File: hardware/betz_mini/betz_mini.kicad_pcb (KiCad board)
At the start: 2 copper layers, 17 parts, among them U1 stm32g474ceu6, U2 AS5047U, U3 IIS328DQ, U4 MP6540

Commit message: WIP
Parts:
- removed R5: 4k7, Resistor_SMD:R_0402_1005Metric
- added C7: 15p, Capacitor_SMD:C_0402_1005Metric, F.Cu at (144.5, 98.5)
- added C8: 100n, Capacitor_SMD:C_0402_1005Metric, F.Cu at (145.5, 85.5)
- added H1: MountingHole_Pad, MountingHole:MountingHole_2.2mm_M2_DIN965_Pad, F.Cu at (140.0, 90.0)
- added H2: MountingHole_Pad, MountingHole:MountingHole_2.2mm_M2_DIN965_Pad, F.Cu at (160.0, 90.0)
- added H3: MountingHole_Pad, MountingHole:MountingHole_2.2mm_M2_DIN965_Pad, F.Cu at (140.0, 110.0)
- added H4: MountingHole_Pad, MountingHole:MountingHole_2.2mm_M2_DIN965_Pad, F.Cu at (160.0, 110.0)
- added J1: upstairs, Connector_PinHeader_2.00mm:PinHeader_2x06_P2.00mm_Vertical, F.Cu at (135.5, 95.0)
- added J2: Conn_ARM_JTAG_SWD_10, Connector_PinHeader_1.27mm:PinHeader_2x05_P1.27mm_Vertical, F.Cu at (152.5, 84.5)
- added X1: 8 MHz, Crystal:Crystal_SMD_5032-2Pin_5.0x3.2mm, F.Cu at (142.0, 97.0)
- C4, C5: value 10u -> 22u
- C6: value 10u -> 15p; footprint Capacitor_SMD:C_1210_3225Metric -> Capacitor_SMD:C_0402_1005Metric
- U2: moved to B.Cu
- moved U4 29.6 mm to (148.5, 110.5), turned to -90 degrees
- moved C2 28.9 mm to (151.0, 114.5), turned to 0 degrees
- moved C1 27.5 mm to (152.5, 112.0), turned to -90 degrees
- moved C3 27.1 mm to (145.5, 114.5), turned to 180 degrees
- moved C6 26.3 mm to (144.5, 95.5), turned to -90 degrees
- moved R6 24.4 mm to (156.0, 98.5), turned to -90 degrees
- moved R3 19.0 mm to (157.5, 98.5), turned to -90 degrees
- moved R4 18.7 mm to (157.5, 100.5), turned to -90 degrees
- moved R1 17.3 mm to (159.0, 98.5), turned to -90 degrees
- moved R2 17.3 mm to (159.0, 100.5), turned to -90 degrees
- moved R7 17.2 mm to (156.0, 100.5), turned to -90 degrees
- moved C4 16.0 mm to (155.0, 113.0), turned to -90 degrees
- moved C5 14.7 mm to (155.0, 108.0)
- moved U3 14.0 mm to (163.0, 101.5)
- moved U2 13.5 mm to (150.0, 100.0)
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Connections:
- net Net-(C1-Pad2) renamed /VCP
- net Net-(C2-Pad1) renamed /CP1
- net Net-(C2-Pad2) renamed /CP2
- net Net-(C3-Pad1) renamed /VG
- C6 pad 1: VBUS -> Net-(C6-Pad1)
- U1 pad 1: Net-(U1-Pad1) -> +3V3
- U1 pad 23: Net-(U1-Pad23) -> +3V3
- U1 pad 35: Net-(U1-Pad35) -> +3V3
- U1 pad 36: Net-(U1-Pad36) -> /SWDIO
- U1 pad 37: Net-(U1-Pad37) -> /SWCLK
- U1 pad 48: Net-(U1-Pad48) -> +3V3
- U1 pad 5: Net-(U1-Pad5) -> Net-(C6-Pad1)
- U1 pad 7: Net-(U1-Pad7) -> /NRST
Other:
- board outline added: 35 x 35 mm
- copper layers 2 -> 4

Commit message: WIP. 35mm square
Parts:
- added REF**: Molex_Nano-Fit_105313-xx04_1x04_P2.50mm_Horizontal, Connector_Molex:Molex_Nano-Fit_105313-xx04_1x04_P2.50mm_Horizontal, B.Cu at (142.5, 93.0)
- added REF**: Molex_Nano-Fit_105313-xx04_1x04_P2.50mm_Horizontal, Connector_Molex:Molex_Nano-Fit_105313-xx04_1x04_P2.50mm_Horizontal, B.Cu at (142.5, 105.0)
- added REF**: Molex_Nano-Fit_105313-xx03_1x03_P2.50mm_Horizontal, Connector_Molex:Molex_Nano-Fit_105313-xx03_1x03_P2.50mm_Horizontal, B.Cu at (142.5, 114.5)
- C4: moved to B.Cu
- U2: moved to F.Cu
- moved C4 25.5 mm to (136.5, 95.5), turned to 180 degrees
- moved X1 23.6 mm to (165.5, 95.0), turned to 90 degrees
- moved C7 22.3 mm to (165.5, 91.0), turned to 0 degrees
- moved C6 21.3 mm to (165.5, 99.0), turned to 0 degrees
- moved C8 20.5 mm to (165.5, 90.0), turned to 0 degrees
- moved J2 19.6 mm to (134.0, 91.0), turned to 90 degrees
- moved R6 17.5 mm to (157.0, 116.0), turned to 0 degrees
- moved U3 16.6 mm to (158.5, 85.5), turned to 180 degrees
- moved R3 16.0 mm to (157.0, 114.5), turned to 0 degrees
- moved R7 15.8 mm to (159.0, 116.0), turned to 0 degrees
- moved R1 14.6 mm to (157.0, 113.0), turned to 0 degrees
- moved R4 14.1 mm to (159.0, 114.5), turned to 0 degrees
- moved R2 12.5 mm to (159.0, 113.0), turned to 0 degrees
- moved C1 10.1 mm to (162.0, 108.5)
- moved C2 10.1 mm to (160.5, 111.0)
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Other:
- outline, holes or cut-outs redrawn

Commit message: WIP detailing schematic and placement
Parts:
- removed REF** (x2): Molex_Nano-Fit_105313-xx04_1x04_P2.50mm_Horizontal, Connector_Molex:Molex_Nano-Fit_105313-xx04_1x04_P2.50mm_Horizontal
- removed REF**: Molex_Nano-Fit_105313-xx03_1x03_P2.50mm_Horizontal, Connector_Molex:Molex_Nano-Fit_105313-xx03_1x03_P2.50mm_Horizontal
- added C10: 10u, Capacitor_SMD:C_1210_3225Metric, B.Cu at (150.0, 115.0)
- added C11: 47u, Capacitor_SMD:C_1210_3225Metric, B.Cu at (138.5, 99.0)
- added C9: 470u, Capacitor_THT:C_Radial_D8.0mm_H11.5mm_P3.50mm, B.Cu at (138.0, 103.5)
- added J2: downstream, Connector_Molex:Molex_Nano-Fit_105314-xx04_2x02_P2.50mm_Horizontal, B.Cu at (142.0, 100.5)
- added J4: BLDC, Connector_Molex:Molex_Nano-Fit_105313-xx03_1x03_P2.50mm_Horizontal, B.Cu at (144.5, 111.0)
- added U5: LMZM23601V3, Package_LGA:Texas_SIL0010A_MicroSiP-10-1EP_3.8x3mm_P0.6mm_EP0.7x2.9mm_ThermalVias, B.Cu at (138.5, 95.0)
- J1: value upstairs -> upstream; footprint Connector_PinHeader_2.00mm:PinHeader_2x06_P2.00mm_Vertical -> Connector_Molex:Molex_Nano-Fit_105314-xx04_2x02_P2.50mm_Horizontal; moved to B.Cu
- J3: renamed from J2; value Conn_ARM_JTAG_SWD_10 -> ARM SWD; moved to B.Cu
- moved U3 23.6 mm to (160.5, 109.0)
- moved J3 15.0 mm to (147.5, 84.5), turned to -90 degrees
- moved C6 12.1 mm to (160.5, 88.0), turned to 180 degrees
- moved C8 11.0 mm to (154.5, 91.0), turned to 90 degrees
- moved R1 10.7 mm to (159.0, 102.5)
- moved R2 10.7 mm to (161.0, 102.5)
- moved R3 10.7 mm to (159.0, 104.0)
- moved R4 10.7 mm to (161.0, 104.0)
- moved R6 10.7 mm to (159.0, 105.5)
- moved R7 10.7 mm to (161.0, 105.5)
- moved C7 10.0 mm to (155.5, 91.0), turned to 90 degrees
- moved J1 9.92 mm to (142.0, 92.5)
- moved H4 9.06 mm to (155.5, 113.5)
- moved C1 8.63 mm to (153.5, 110.0)
- moved C2 8.63 mm to (152.0, 112.5)
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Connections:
- net /RX renamed Net-(J1-Pad3)
- J1 pad 1: +3V3 -> VBUS
- J1 pad 2: /TX -> GND
- J1 pad 4: GND -> Net-(J1-Pad4)
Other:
- outline, holes or cut-outs redrawn

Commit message: WIP schematic
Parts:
- added D1: status, LED_SMD:LED_0402_1005Metric, B.Cu at (166.0, 103.5)
- added J5: debug, Connector_PinHeader_2.54mm:PinHeader_1x02_P2.54mm_Vertical, F.Cu at (134.0, 84.5)
- added R5: 330, Resistor_SMD:R_0402_1005Metric, B.Cu at (165.0, 103.5)
- added U6: THVD2450, Package_SO:VSSOP-8_3.0x3.0mm_P0.65mm, F.Cu at (149.0, 91.5)
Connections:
- J1 pad 3: Net-(J1-Pad3) -> /RS485_B
- J1 pad 4: Net-(J1-Pad4) -> /RS485_A
- J2 pad 3: Net-(J2-Pad3) -> /RS485_B
- J2 pad 4: Net-(J2-Pad4) -> /RS485_A

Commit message: WIP awesome
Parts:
- J5: value debug -> BONUS; footprint Connector_PinHeader_2.54mm:PinHeader_1x02_P2.54mm_Vertical -> Connector_PinHeader_1.27mm:PinHeader_1x08_P1.27mm_Horizontal
- moved J5 33.4 mm to (165.5, 95.5)
- moved D1 29.8 mm to (140.5, 88.0)
- moved R5 29.8 mm to (139.5, 88.0)
- moved U1 1.00 mm to (158.5, 97.5)
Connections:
- J5 pad 2: GND -> Net-(J5-Pad2)

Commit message: WIP betz mini
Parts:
- added C12: 100n, Capacitor_SMD:C_0402_1005Metric, F.Cu at (144.5, 93.0)
- added C13: 100n, Capacitor_SMD:C_0402_1005Metric, F.Cu at (164.0, 105.0)
- added C14: 100n, Capacitor_SMD:C_0402_1005Metric, F.Cu at (156.5, 95.0)
- added C15: 100n, Capacitor_SMD:C_0402_1005Metric, F.Cu at (155.5, 103.0)
- added C16: 100n, Capacitor_SMD:C_0402_1005Metric, F.Cu at (151.0, 104.5)
- added C17: 100u, Capacitor_THT:C_Radial_D6.3mm_H11.0mm_P2.50mm, B.Cu at (133.5, 93.5)
- added C18: 100n, Capacitor_SMD:C_0402_1005Metric, F.Cu at (152.0, 109.0)
- added C19: 1u, Capacitor_SMD:C_0402_1005Metric, F.Cu at (153.0, 109.0)
- added C20: 10u, Capacitor_SMD:C_0402_1005Metric, F.Cu at (158.5, 93.0)
- added C21: 1u, Capacitor_SMD:C_0402_1005Metric, F.Cu at (158.5, 94.0)
- added C22: 1u, Capacitor_SMD:C_0402_1005Metric, F.Cu at (160.5, 94.0)
- added C23: 100n, Capacitor_SMD:C_0402_1005Metric, F.Cu at (158.5, 95.0)
- added C24: 100n, Capacitor_SMD:C_0402_1005Metric, F.Cu at (160.5, 95.0)
- added C25: 10u, Capacitor_SMD:C_0402_1005Metric, F.Cu at (164.0, 106.0)
- added C26: 1u, Capacitor_SMD:C_0402_1005Metric, F.Cu at (144.5, 94.0)
- added C27: 100n, Capacitor_SMD:C_0402_1005Metric, F.Cu at (149.5, 87.0)
- added R10: ferrite, Resistor_SMD:R_0402_1005Metric, F.Cu at (158.5, 92.0)
- added R11: 100k, Resistor_SMD:R_0402_1005Metric, F.Cu at (147.5, 87.0)
- added R12: 4k7, Resistor_SMD:R_0402_1005Metric, F.Cu at (149.5, 88.0)
- added R8: 4k7, Resistor_SMD:R_0402_1005Metric, F.Cu at (147.5, 106.5)
- added R9: 4k7, Resistor_SMD:R_0402_1005Metric, F.Cu at (145.0, 109.5)
- C10, C11, C4, D1, R5, U5: moved to F.Cu
- C9: value 470u -> 100u; footprint Capacitor_THT:C_Radial_D8.0mm_H11.5mm_P3.50mm -> Capacitor_THT:C_Radial_D6.3mm_H11.0mm_P2.50mm
- J5: footprint Connector_PinHeader_1.27mm:PinHeader_1x08_P1.27mm_Horizontal -> Connector_PinHeader_1.27mm:PinHeader_1x08_P1.27mm_Vertical; moved to B.Cu
- moved J3 34.4 mm to (152.5, 118.5), turned to 90 degrees
- moved R5 34.0 mm to (162.5, 113.0), turned to 0 degrees
- moved D1 32.6 mm to (162.5, 112.0), turned to 180 degrees
- moved C8 28.0 mm to (145.5, 117.5), turned to -90 degrees
- moved J5 27.6 mm to (145.5, 114.5), turned to -90 degrees
- moved C10 24.7 mm to (132.5, 97.5), turned to 90 degrees
- moved C5 24.1 mm to (132.5, 102.5), turned to -90 degrees
- moved C2 23.7 mm to (135.5, 95.5), turned to 180 degrees
- moved C1 22.3 mm to (138.0, 94.0)
- moved C11 21.6 mm to (154.0, 84.0), turned to 90 degrees
- moved C3 19.2 mm to (140.5, 95.5), turned to 0 degrees
- moved C6 17.9 mm to (167.5, 104.5), turned to 0 degrees
- moved U5 15.9 mm to (150.0, 84.0), turned to 0 degrees
- moved R1 14.4 mm to (162.5, 88.5)
- moved R2 14.4 mm to (164.5, 88.5)
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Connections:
- J5 pad 1: /DEBUG_TX -> GND
- J5 pad 2: Net-(J5-Pad2) -> +3V3
- J5 pad 3: Net-(J5-Pad3) -> /DEBUG_TX
- J5 pad 4: Net-(J5-Pad4) -> /BONUS_MOSI
- J5 pad 5: Net-(J5-Pad5) -> /BONUS_MISO
- J5 pad 6: Net-(J5-Pad6) -> /BONUS_SCK
- J5 pad 7: Net-(J5-Pad7) -> /BONUS_GPIO
- J5 pad 8: GND -> /BONUS_CS
- U1 pad 10: Net-(U1-Pad10) -> /RS485_DI
- U1 pad 11: Net-(U1-Pad11) -> /RS485_RO
- U1 pad 15: Net-(U1-Pad15) -> /IB
- U1 pad 18: Net-(U1-Pad18) -> /IA
- U1 pad 24: Net-(U1-Pad24) -> /ENC_CS
- U1 pad 25: Net-(U1-Pad25) -> /VBUS_DIV
- U1 pad 26: Net-(U1-Pad26) -> /ENC_SCK
- U1 pad 27: Net-(U1-Pad27) -> /ENC_MISO
- U1 pad 28: Net-(U1-Pad28) -> /ENC_MOSI
- U1 pad 29: Net-(U1-Pad29) -> /BLDC_EN
- U1 pad 30: Net-(U1-Pad30) -> /PWMC
- U1 pad 31: Net-(U1-Pad31) -> /PWMB
- U1 pad 32: Net-(U1-Pad32) -> /PWMA
- U1 pad 33: Net-(U1-Pad33) -> /SLEEP
- U1 pad 34: Net-(U1-Pad34) -> /FAULT
- U1 pad 38: Net-(U1-Pad38) -> /ACCEL_SCL
- U1 pad 39: Net-(U1-Pad39) -> /BONUS_SCK
- U1 pad 40: Net-(U1-Pad40) -> /BONUS_MISO
- U1 pad 41: Net-(U1-Pad41) -> /BONUS_GPIO
- U1 pad 42: Net-(U1-Pad42) -> /BONUS_CS
- U1 pad 43: Net-(U1-Pad43) -> /BONUS_MOSI
- U1 pad 44: Net-(U1-Pad44) -> /DEBUG_TX
- U1 pad 45: Net-(U1-Pad45) -> /ACCEL_SDA
- U1 pad 46: Net-(U1-Pad46) -> GND
- U1 pad 47: Net-(U1-Pad47) -> /STATUS_LED
- U1 pad 49: Net-(U1-Pad49) -> GND
- U1 pad 8: Net-(U1-Pad8) -> /IC
- U1 pad 9: Net-(U1-Pad9) -> /RS485_DE
- U2 pad 1: Net-(U2-Pad1) -> /ENC_CS
- U2 pad 11: Net-(U2-Pad11) -> +3V3
- U2 pad 12: Net-(U2-Pad12) -> +3V3
- U2 pad 13: Net-(U2-Pad13) -> GND
- U2 pad 2: Net-(U2-Pad2) -> /ENC_SCK
- U2 pad 3: Net-(U2-Pad3) -> /ENC_MISO
- U2 pad 4: Net-(U2-Pad4) -> /ENC_MOSI
- U2 pad 5: Net-(U2-Pad5) -> GND
- U3 pad 10: Net-(U3-Pad10) -> GND
- U3 pad 11: Net-(U3-Pad11) -> /ACCEL_SCL
- U3 pad 12: Net-(U3-Pad12) -> +3V3
- U3 pad 13: Net-(U3-Pad13) -> +3V3
- U3 pad 14: Net-(U3-Pad14) -> +3V3
- U3 pad 15: Net-(U3-Pad15) -> GND
- U3 pad 16: Net-(U3-Pad16) -> /ACCEL_SDA
- U3 pad 25: Net-(U3-Pad25) -> GND
- U3 pad 4: Net-(U3-Pad4) -> GND
- U3 pad 5: Net-(U3-Pad5) -> +3V3
- U3 pad 6: Net-(U3-Pad6) -> GND
- U3 pad 8: Net-(U3-Pad8) -> GND
- U3 pad 9: Net-(U3-Pad9) -> GND
- U4 pad 3: /ENA -> /BLDC_EN
- U4 pad 4: /ENB -> /BLDC_EN
- U4 pad 5: /ENC -> /BLDC_EN
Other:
- board size 35 x 35 mm -> 40 x 40 mm

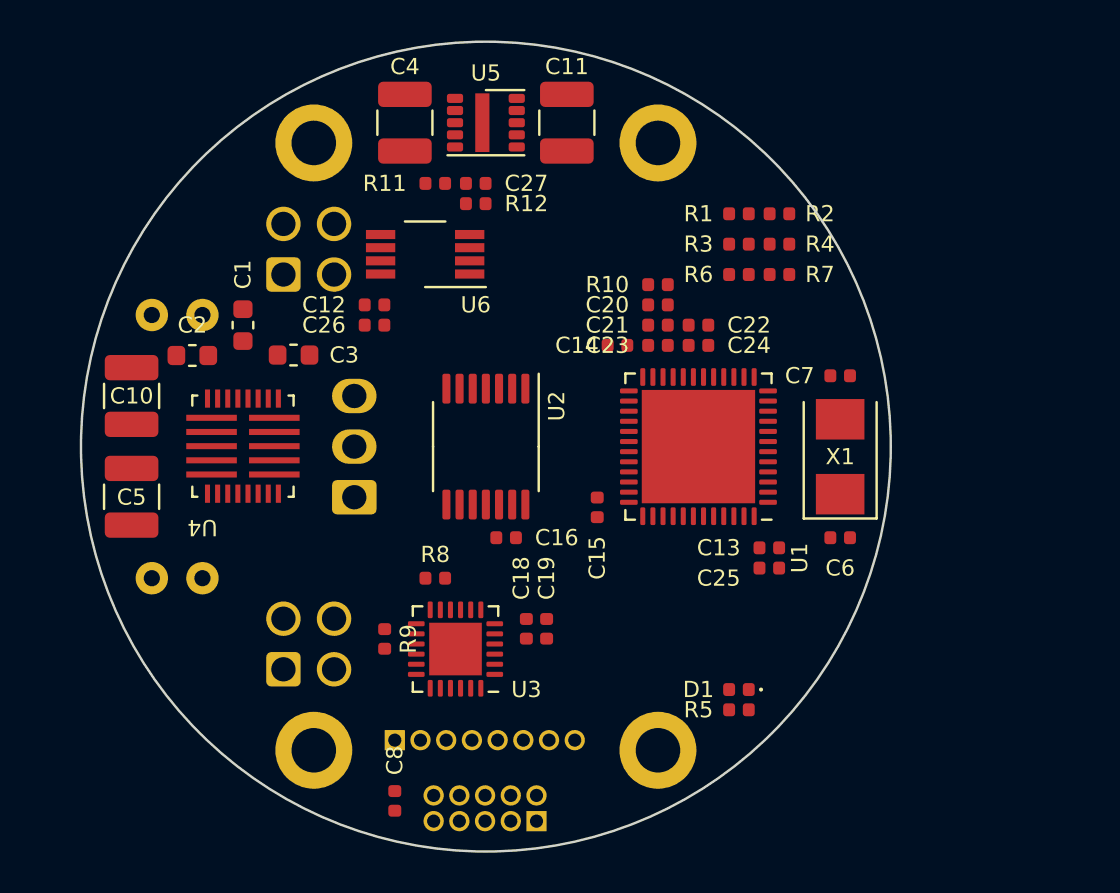
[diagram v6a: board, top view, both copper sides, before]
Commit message: start route of power section
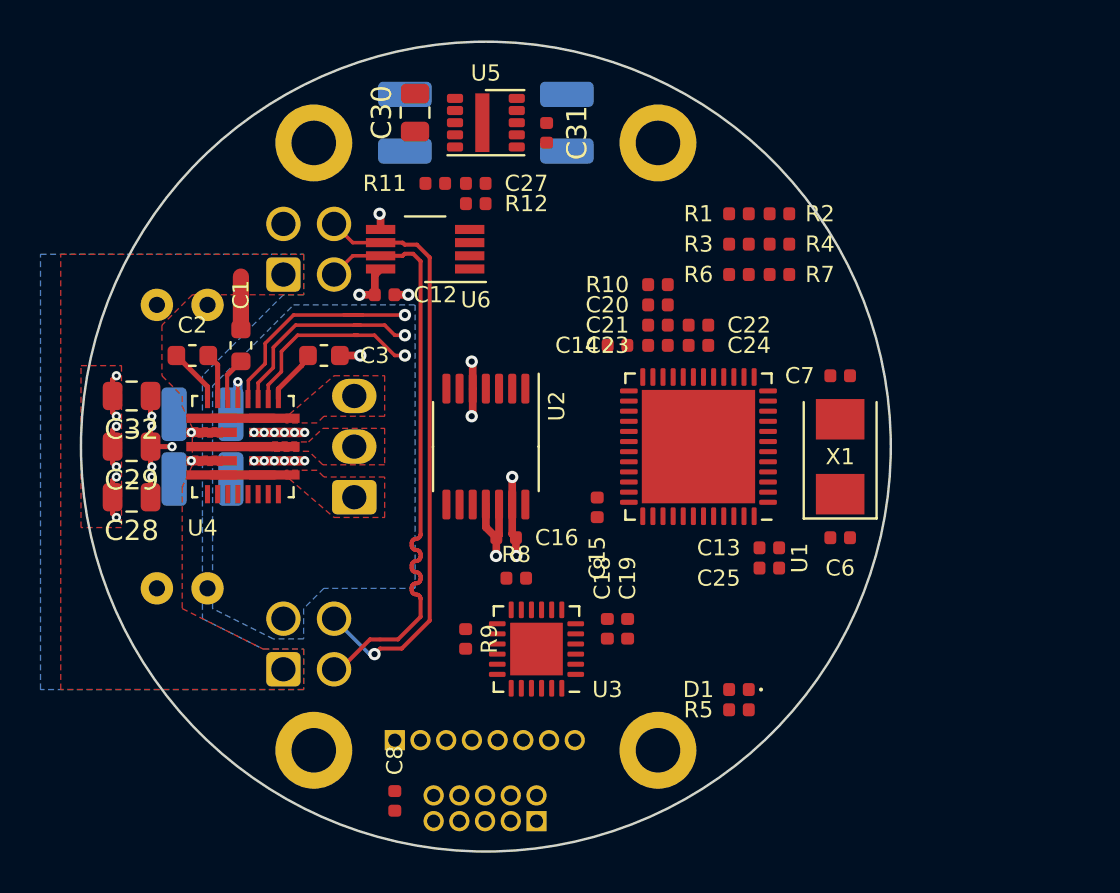
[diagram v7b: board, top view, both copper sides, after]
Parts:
- removed C26: 1u, Capacitor_SMD:C_0402_1005Metric
- added C28: 4u7, Capacitor_SMD:C_0805_2012Metric, F.Cu at (132.5, 102.5)
- added C29: 4u7, Capacitor_SMD:C_0805_2012Metric, F.Cu at (132.5, 100.0)
- added C30: 4u7, Capacitor_SMD:C_0805_2012Metric, F.Cu at (146.5, 83.5)
- added C31: 10u, Capacitor_SMD:C_0402_1005Metric, F.Cu at (153.0, 84.5)
- added C32: 4u7, Capacitor_SMD:C_0805_2012Metric, F.Cu at (132.5, 97.5)
- C10, C11, C4, C5: moved to B.Cu
- moved C18 4.00 mm to (156.0, 109.0)
- moved C19 4.00 mm to (157.0, 109.0)
- moved R8 4.00 mm to (151.5, 106.5)
- moved R9 4.00 mm to (149.0, 109.5)
- moved U3 4.00 mm to (152.5, 110.0)
- moved C10 3.61 mm to (136.0, 98.4), turned to 0 degrees
- moved C5 3.61 mm to (136.0, 101.6), turned to 0 degrees
- moved C3 1.50 mm to (142.0, 95.5)
- moved C1 1.00 mm to (137.9, 95.0)
- moved C12 0.71 mm to (145.0, 92.5), turned to 0 degrees
- moved C17 0.56 mm to (133.8, 93.0)
- moved C9 0.56 mm to (133.8, 107.0)
- moved U6 0.25 mm to (147.0, 90.2)
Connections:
- net /RS485_A renamed /RS485+
- net /RS485_B renamed /RS485-
- J4 pad 1: /SC -> /SA
- J4 pad 3: /SA -> /SC
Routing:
- net /RS485+: track 0.00 -> 29.5 mm, vias 0 -> 1
- net /RS485-: track 0.00 -> 29.3 mm
- net GND: track 0.00 -> 21.3 mm, vias 0 -> 26
- net /IC: track 0.00 -> 11.5 mm, vias 0 -> 1
- net /IB: track 0.00 -> 10.3 mm, vias 0 -> 1
- net VBUS: track 0.00 -> 9.78 mm, vias 0 -> 7
- net /IA: track 0.00 -> 9.64 mm, vias 0 -> 1
- net +3V3: track 0.00 -> 6.61 mm, vias 0 -> 2
- net /SC: track 0.00 -> 3.10 mm
- net /SB: track 0.00 -> 3.10 mm
- net /SA: track 0.00 -> 3.10 mm
- net /CP2: track 0.00 -> 2.79 mm
- net /VG: track 0.00 -> 2.72 mm
- net /CP1: track 0.00 -> 2.34 mm
- net /VCP: track 0.00 -> 2.16 mm
- added copper zone on F.Cu, net /SA
- added copper zone on F.Cu, net /SB
- added copper zone on F.Cu, net /SC
- added copper zone on B.Cu, net GND
- added copper zone on F.Cu, net GND
- added copper zone on In1.Cu, net GND
- added copper zone on B.Cu, net VBUS
- added copper zone on F.Cu, net VBUS
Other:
- rule trace_min: 0.2 -> 0.1524
- rule via_min_drill: 0.3 -> 0.2032

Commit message: rev.A first pass complete
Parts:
- added J6: EXTRA_BONUS, Connector_PinHeader_1.27mm:PinHeader_1x01_P1.27mm_Vertical, B.Cu at (162.9, 95.1)
- added LOGO1: Logo_Open_Hardware_Small, Symbol:OSHW-Logo_7.5x8mm_SilkScreen, B.Cu at (160.2, 100.0)
- moved R8 14.3 mm to (165.5, 109.5), turned to -90 degrees
- moved R9 13.1 mm to (161.6, 106.0), turned to 180 degrees
- moved R2 9.71 mm to (155.9, 93.0), turned to -90 degrees
- moved C8 9.00 mm to (154.5, 117.5), turned to 90 degrees
- moved R7 8.90 mm to (155.9, 89.2), turned to 90 degrees
- moved U3 8.81 mm to (161.3, 109.5), turned to 90 degrees
- moved R4 8.67 mm to (155.9, 91.1), turned to -90 degrees
- moved C18 7.46 mm to (162.3, 113.0), turned to 0 degrees
- moved C19 7.29 mm to (162.3, 114.0), turned to 0 degrees
- moved D1 6.10 mm to (166.0, 107.0), turned to 0 degrees
- moved R5 6.10 mm to (166.0, 108.0), turned to 180 degrees
- moved J3 5.22 mm to (147.5, 117.0), turned to -90 degrees
- moved R1 4.30 mm to (160.0, 92.0)
- moved R6 2.92 mm to (160.0, 90.0)
- moved R3 2.69 mm to (160.0, 91.0)
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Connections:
- J5 pad 3: /DEBUG_TX -> /BONUS_SCK
- J5 pad 4: /BONUS_MOSI -> /BONUS_MISO
- J5 pad 5: /BONUS_MISO -> /BONUS_GPIO
- J5 pad 6: /BONUS_SCK -> /BONUS_CS
- J5 pad 7: /BONUS_GPIO -> /BONUS_MOSI
- J5 pad 8: /BONUS_CS -> /DEBUG_TX
- U1 pad 13: Net-(U1-Pad13) -> /PA5
- U1 pad 2: Net-(U1-Pad2) -> /STATUS_LED
- U1 pad 47: /STATUS_LED -> Net-(U1-Pad47)
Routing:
- net GND: track 21.3 -> 88.7 mm, vias 26 -> 62
- net /NRST: track 0.00 -> 31.9 mm, vias 0 -> 2
- net +3V3: track 6.61 -> 37.9 mm, vias 2 -> 13
- net /BLDC_EN: track 0.00 -> 30.4 mm, vias 0 -> 2
- net /IC: track 11.5 -> 41.6 mm, vias 1 -> 2
- net /RS485_DE: track 0.00 -> 26.7 mm, vias 0 -> 2
- net /SWCLK: track 0.00 -> 25.9 mm
- net /FAULT: track 0.00 -> 25.9 mm, vias 0 -> 2
- net VBUS: track 9.78 -> 35.0 mm, vias 7 -> 19
- net /SLEEP: track 0.00 -> 24.8 mm, vias 0 -> 2
- net /SWDIO: track 0.00 -> 24.8 mm, vias 0 -> 1
- net /IB: track 10.3 -> 34.1 mm, vias 1 -> 4
- net /RS485_DI: track 0.00 -> 23.6 mm, vias 0 -> 2
- net /PWMA: track 0.00 -> 22.5 mm, vias 0 -> 2
- net /IA: track 9.64 -> 31.7 mm, vias 1 -> 4
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- added copper zone on B.Cu, net +3V3
- added copper zone on F.Cu, net +3V3
- added copper zone on In2.Cu, net +3V3
- added copper zone on In2.Cu, net GND
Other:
- net class Default: clearance 0.2 -> 0.1524
- rule trace_clearance: 0.2 -> 0.1524
- board text added: "+24V-"
- board text added: "3V3"
- board text added: "A"
- board text added: "B"
- board text added: "BETZ MINI REV A MAY 2020"
- board text added: "CS"
- board text added: "GND"
- board text added: "MISO"
- board text added: "MOSI"
- board text added: "PB3"
- board text added: "SCK"
- board text added: "TX"
